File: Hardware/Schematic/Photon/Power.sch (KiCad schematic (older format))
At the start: 7 parts, among them U2 L7805

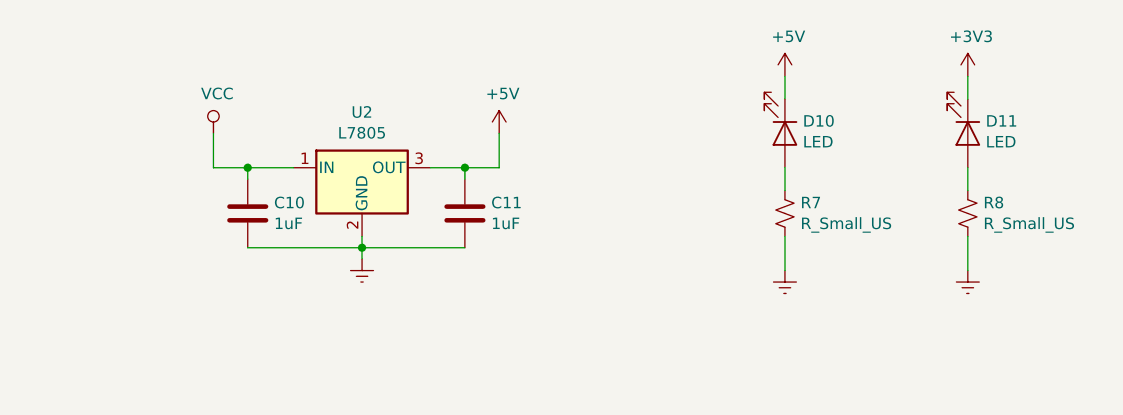
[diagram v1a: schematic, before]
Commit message: Added a barrel jack connector to the photon board
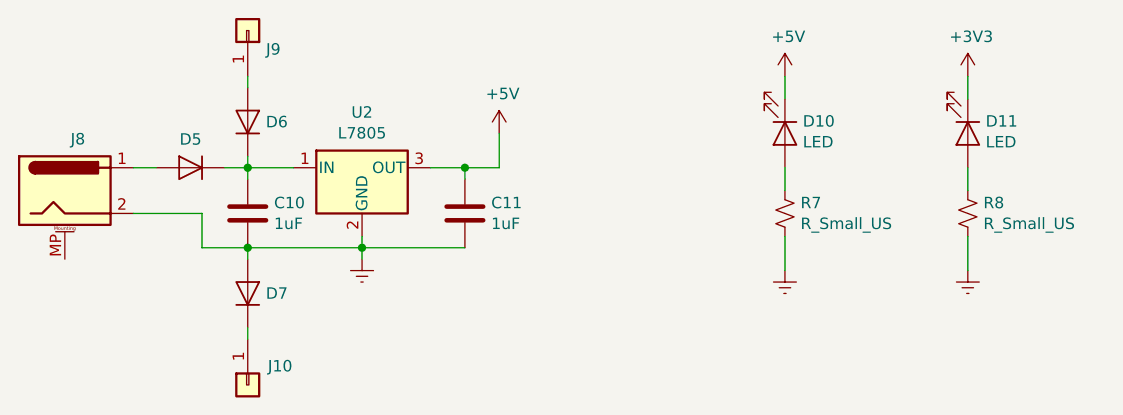
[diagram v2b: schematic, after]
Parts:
- added D5, D6, D7: D, Diode_SMD:D_2512_6332Metric_Pad1.52x3.35mm_HandSolder, symbol Device:D
- added J10, J9: Conn_01x01, TestPoint:TestPoint_Loop_D2.50mm_Drill1.0mm, symbol Connector_Generic:Conn_01x01
- added J8: Barrel_Jack_MountingPin, Connector_BarrelJack:BarrelJack_CUI_PJ-063AH_Horizontal, symbol Connector:Barrel_Jack_MountingPin
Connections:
- net Earth: now also D7.2 (A), J8.2
- net VCC: no longer names the net of C10.1, U2.1 (IN)
- net VCC: now also D5.1 (K), D6.1 (K)
- new net: D5.2 (A), J8.1
- new net: D6.2 (A), J9.1 (Pin_1)
- new net: D7.1 (K), J10.1 (Pin_1)
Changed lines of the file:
@@
 $Descr A4 11693 8268
 encoding utf-8
-Sheet 6 5
+Sheet 4 4
 Title ""
 Date ""
@@
 Wire Wire Line
 	4600 2500 4600 2350
-$Comp
-L power:VCC #PWR0131
-U 1 1 5D21D766
-P 3350 2350
-F 0 "#PWR0131" H 3350 2200 50  0001 C CNN
-F 1 "VCC" H 3367 2523 50  0000 C CNN
-F 2 "" H 3350 2350 50  0001 C CNN
-F 3 "" H 3350 2350 50  0001 C CNN
-	1    3350 2350
-	1    0    0    -1
-$EndComp
 Wire Wire Line
 	3700 2500 3500 2500
-Wire Wire Line
-	3350 2500 3350 2350
 $Comp
 L power:Earth #PWR0132
@@
 	4000 2850 4000 2800
 Wire Wire Line
-	4000 2850 3500 2850
-Wire Wire Line
 	4450 2550 4450 2500
 Connection ~ 4450 2500
@@
 Wire Wire Line
 	3500 2550 3500 2500
-Connection ~ 3500 2500
-Wire Wire Line
-	3500 2500 3350 2500
 $Comp
 L Device:R_Small_US R7
@@
 Wire Wire Line
 	5850 2200 5850 2100
+$Comp
+L Device:D D5
+U 1 1 5D074735
+P 3250 2500
+F 0 "D5" H 3250 2624 50  0000 C CNN
+F 1 "D" H 3250 2625 50  0001 C CNN
+F 2 "Diode_SMD:D_2512_6332Metric_Pad1.52x3.35mm_HandSolder" H 3250 2500 50  0001 C CNN
+F 3 "~" H 3250 2500 50  0001 C CNN
+	1    3250 2500
+	-1   0    0    -1
+$EndComp
+Connection ~ 3500 2850
+Connection ~ 3500 2500
+$Comp
+L Connector_Generic:Conn_01x01 J9
+U 1 1 5D0781A8
+P 3500 1900
+F 0 "J9" V 3418 1980 50  0000 L CNN
+F 1 "Conn_01x01" V 3373 1980 50  0001 L CNN
+F 2 "TestPoint:TestPoint_Loop_D2.50mm_Drill1.0mm" H 3500 1900 50  0001 C CNN
+F 3 "~" H 3500 1900 50  0001 C CNN
+	1    3500 1900
+	0    1    -1   0
+$EndComp
+$Comp
+L Connector_Generic:Conn_01x01 J10
+U 1 1 5D079B5B
+P 3500 3450
+F 0 "J10" V 3418 3362 50  0000 R CNN
+F 1 "Conn_01x01" V 3463 3362 50  0001 R CNN
+F 2 "TestPoint:TestPoint_Loop_D2.50mm_Drill1.0mm" H 3500 3450 50  0001 C CNN
+F 3 "~" H 3500 3450 50  0001 C CNN
+	1    3500 3450
+	0    -1   1    0
+$EndComp
+$Comp
+L Device:D D6
+U 1 1 5D07C1C3
+P 3500 2300
+F 0 "D6" V 3500 2379 50  0000 L CNN
+F 1 "D" H 3500 2425 50  0001 C CNN
+F 2 "Diode_SMD:D_2512_6332Metric_Pad1.52x3.35mm_HandSolder" H 3500 2300 50  0001 C CNN
+F 3 "~" H 3500 2300 50  0001 C CNN
+	1    3500 2300
+	0    1    -1   0
+$EndComp
+$Comp
+L Device:D D7
+U 1 1 5D07FB85
+P 3500 3050
+F 0 "D7" V 3500 3129 50  0000 L CNN
+F 1 "D" H 3500 3175 50  0001 C CNN
+F 2 "Diode_SMD:D_2512_6332Metric_Pad1.52x3.35mm_HandSolder" H 3500 3050 50  0001 C CNN
+F 3 "~" H 3500 3050 50  0001 C CNN
+	1    3500 3050
+	0    1    -1   0
+$EndComp
+Wire Wire Line
+	3500 2900 3500 2850
+Wire Wire Line
+	3500 2500 3500 2450
+Wire Wire Line
+	3500 2150 3500 2100
+Wire Wire Line
+	3500 3200 3500 3250
+Wire Wire Line
+	3500 2850 4000 2850
+Wire Wire Line
+	3400 2500 3500 2500
+$Comp
+L Connector:Barrel_Jack_MountingPin J8
+U 1 1 5D071780
+P 2700 2600
+F 0 "J8" H 2757 2825 50  0000 C CNN
+F 1 "Barrel_Jack_MountingPin" H 2757 2826 50  0001 C CNN
+F 2 "Connector_BarrelJack:BarrelJack_CUI_PJ-063AH_Horizontal" H 2750 2560 50  0001 C CNN
+F 3 "~" H 2750 2560 50  0001 C CNN
+	1    2700 2600
+	1    0    0    -1
+$EndComp
+Wire Wire Line
+	3000 2500 3100 2500
+Wire Wire Line
+	3000 2700 3300 2700
+Wire Wire Line
+	3300 2700 3300 2850
+Wire Wire Line
+	3300 2850 3500 2850
 $EndSCHEMATC
